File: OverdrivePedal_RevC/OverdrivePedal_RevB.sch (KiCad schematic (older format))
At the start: 25 parts, among them J1 AudioJack2-Connector, J2 Barrel_Jack, J3 Conn_01x05, J4 SW_SPST, J6 AudioJack2-Connector, U1 DG468DV_T1_E3, U2 TL071, U4 DG468DV_T1_E3, U5 STM32L011D4Px, U6 DG468DV_T1_E3

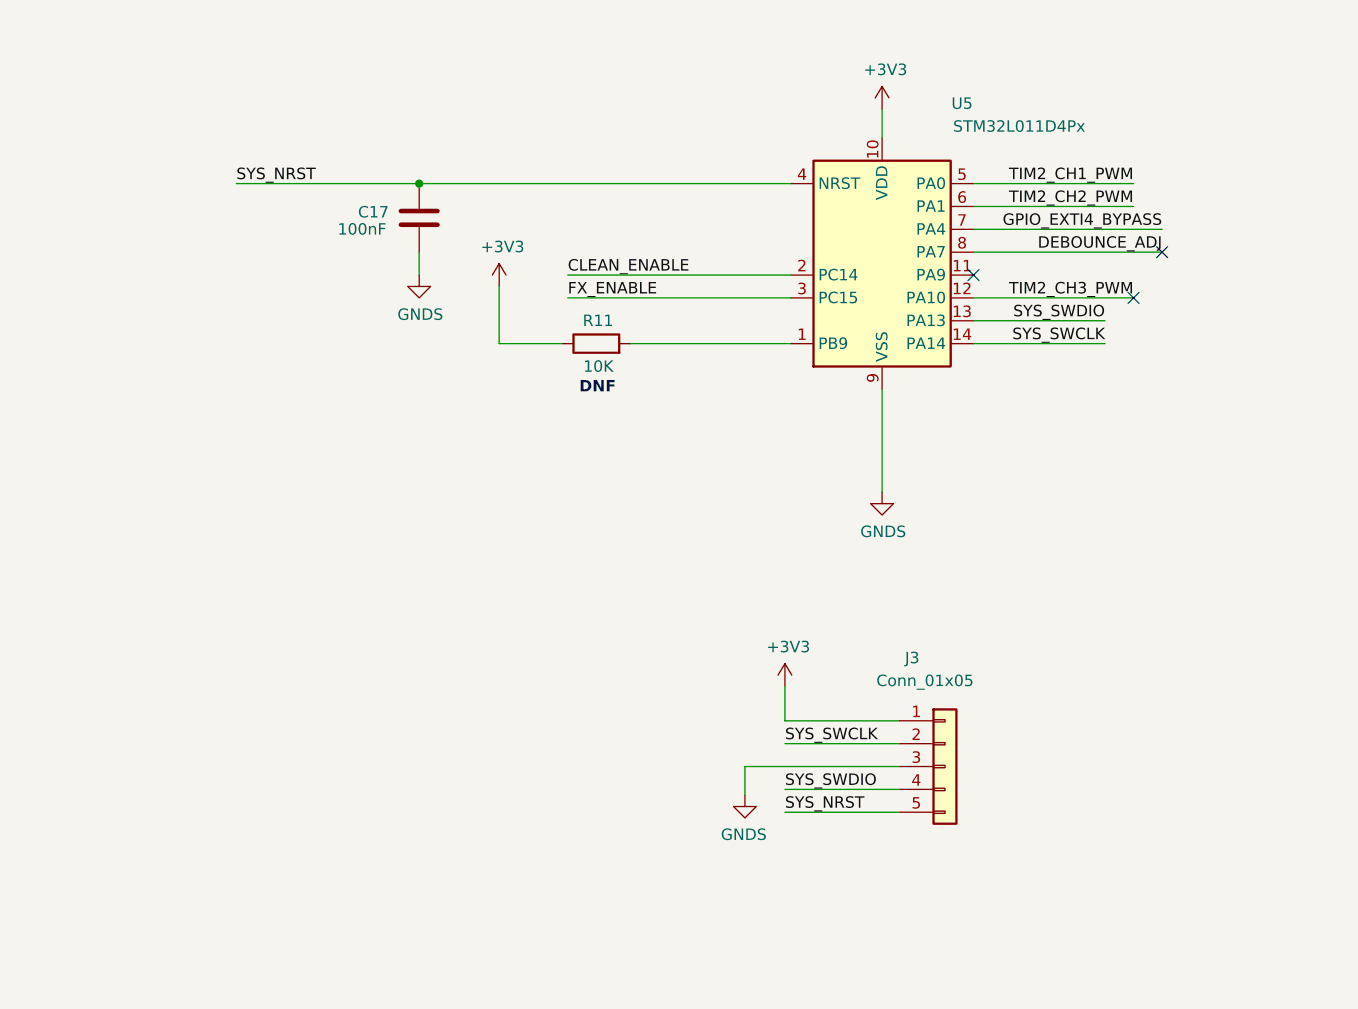
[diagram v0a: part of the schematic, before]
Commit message: updated revc
- Switch PC15 to PA9 for FX_ENABLE
- connected BOOT0 to GND
- Removed U11 charge pump (not required/causing oscillation)
- lowered U3 charge pump LP filter cuttoff to 1.6KHz
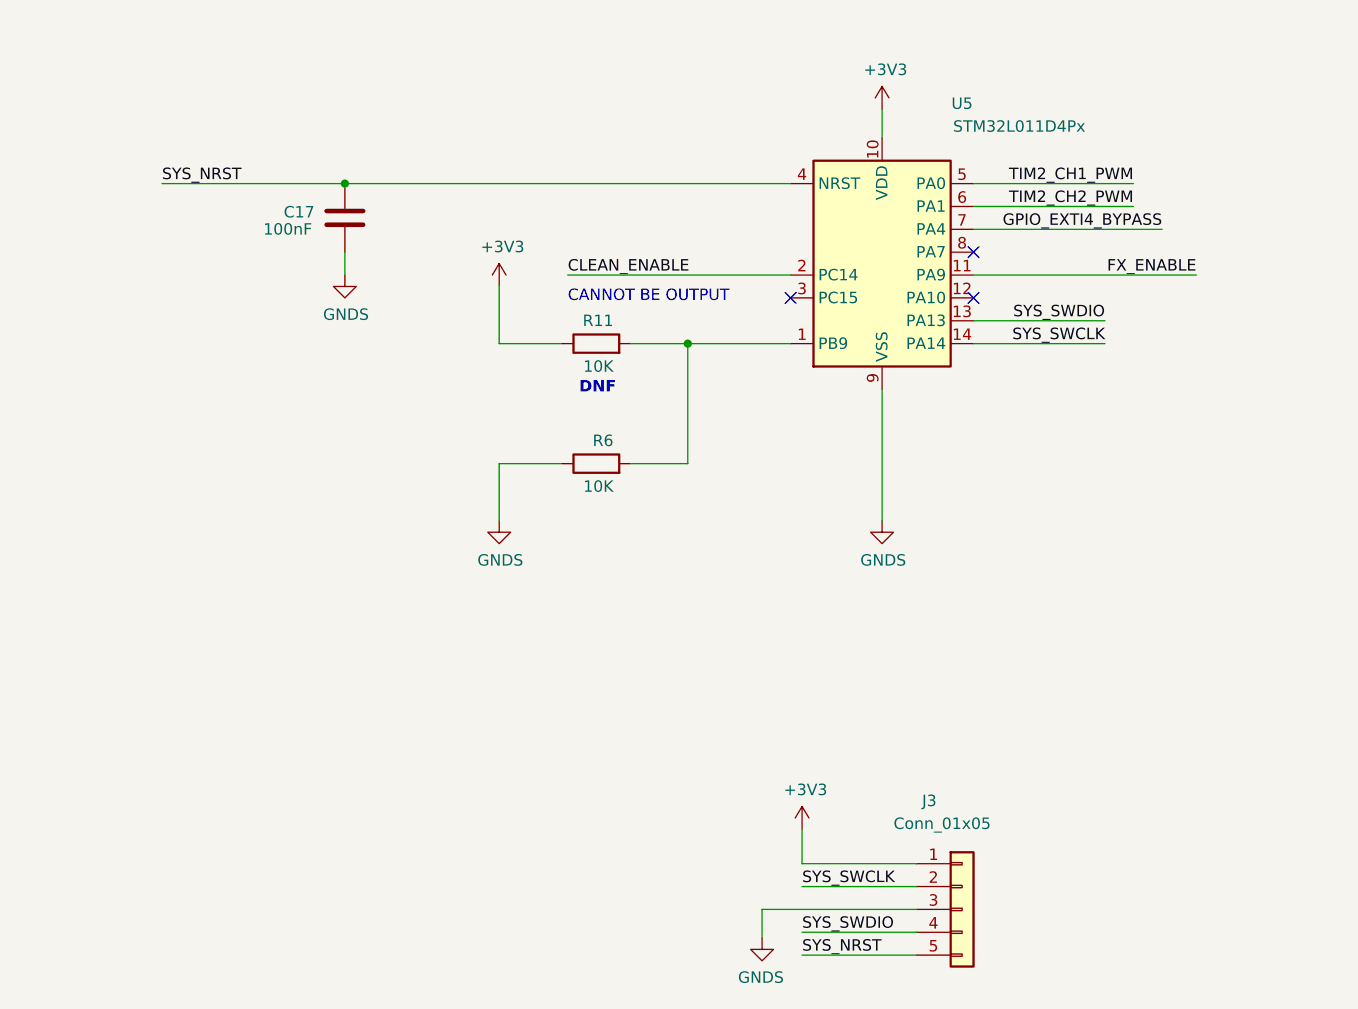
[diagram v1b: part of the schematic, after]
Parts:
- added R6: 10K, Resistor_SMD:R_0402_1005Metric, symbol Device:R
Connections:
- net FX_ENABLE: now also U5.11 (PA9); no longer U5.3 (PC15)
- net GNDS: now also R6.1
- net at R11.2, U5.1 (PB9): now also R6.2
- net DEBOUNCE_ADJ: no longer names the net of U5.8 (PA7)
- net TIM2_CH3_PWM: no longer names the net of U5.12 (PA10)
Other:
- note added: "CANNOT BE OUTPUT"
- moved on the sheet: C17, J3
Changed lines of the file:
@@
 Title "Microcontroller"
 Date "2020-04-10"
-Rev "RevB"
+Rev "RevC"
 Comp ""
-Comment1 "PC15 must be initialised HIGH to prevent debugger lockup"
+Comment1 ""
 Comment2 ""
 Comment3 ""
@@
 L power:GNDS #PWR026
 U 1 1 5F03E5C2
-P 8600 8425
-F 0 "#PWR026" H 8600 8175 50  0001 C CNN
-F 1 "GNDS" H 8605 8252 50  0000 C CNN
-F 2 "" H 8600 8425 50  0001 C CNN
-F 3 "" H 8600 8425 50  0001 C CNN
-	1    8600 8425
-	1    0    0    -1
-$EndComp
-Wire Wire Line
-	9000 7575 9700 7575
-Text Label 9700 7575 2    50   ~ 0
-TIM2_CH3_PWM
+P 8600 8550
+F 0 "#PWR026" H 8600 8300 50  0001 C CNN
+F 1 "GNDS" H 8605 8377 50  0000 C CNN
+F 2 "" H 8600 8550 50  0001 C CNN
+F 3 "" H 8600 8550 50  0001 C CNN
+	1    8600 8550
+	1    0    0    -1
+$EndComp
 Wire Wire Line
 	9000 7775 9575 7775
@@
 Text Label 9825 7275 2    50   ~ 0
 GPIO_EXTI4_BYPASS
-NoConn ~ 9000 7475
 Text Label 7225 7475 0    50   ~ 0
 CLEAN_ENABLE
-Text Label 7225 7575 0    50   ~ 0
+Text Label 9975 7475 2    50   ~ 0
 FX_ENABLE
 $Comp
@@
 L Connector_Generic:Conn_01x05 J3
 U 1 1 5F17BC8C
-P 8875 9625
-F 0 "J3" H 8700 10100 50  0000 L CNN
-F 1 "Conn_01x05" H 8575 10000 50  0000 L CNN
-F 2 "Connector_PinSocket_2.54mm:PinSocket_1x05_P2.54mm_Vertical" H 8875 9625 50  0001 C CNN
-F 3 "~" H 8875 9625 50  0001 C CNN
-	1    8875 9625
-	1    0    0    -1
-$EndComp
-Wire Wire Line
-	8675 9425 8175 9425
-Wire Wire Line
-	8675 9525 8175 9525
-Wire Wire Line
-	8675 9625 8000 9625
-Wire Wire Line
-	8675 9725 8175 9725
-Wire Wire Line
-	8675 9825 8175 9825
-Wire Wire Line
-	8175 9275 8175 9425
+P 8950 10250
+F 0 "J3" H 8775 10725 50  0000 L CNN
+F 1 "Conn_01x05" H 8650 10625 50  0000 L CNN
+F 2 "Connector_PinSocket_2.54mm:PinSocket_1x05_P2.54mm_Vertical" H 8950 10250 50  0001 C CNN
+F 3 "~" H 8950 10250 50  0001 C CNN
+	1    8950 10250
+	1    0    0    -1
+$EndComp
+Wire Wire Line
+	8750 10050 8250 10050
+Wire Wire Line
+	8750 10150 8250 10150
+Wire Wire Line
+	8750 10250 8075 10250
+Wire Wire Line
+	8750 10350 8250 10350
+Wire Wire Line
+	8750 10450 8250 10450
+Wire Wire Line
+	8250 9900 8250 10050
 $Comp
 L power:+3V3 #PWR034
 U 1 1 5F18C62E
-P 8175 9275
-F 0 "#PWR034" H 8175 9125 50  0001 C CNN
-F 1 "+3V3" H 8190 9448 50  0000 C CNN
-F 2 "" H 8175 9275 50  0001 C CNN
-F 3 "" H 8175 9275 50  0001 C CNN
-	1    8175 9275
-	1    0    0    -1
-$EndComp
-Wire Wire Line
-	8000 9625 8000 9750
+P 8250 9900
+F 0 "#PWR034" H 8250 9750 50  0001 C CNN
+F 1 "+3V3" H 8265 10073 50  0000 C CNN
+F 2 "" H 8250 9900 50  0001 C CNN
+F 3 "" H 8250 9900 50  0001 C CNN
+	1    8250 9900
+	1    0    0    -1
+$EndComp
+Wire Wire Line
+	8075 10250 8075 10375
 $Comp
 L power:GNDS #PWR?
 U 1 1 5F18FF3A
-P 8000 9750
+P 8075 10375
 AR Path="/5E6165F4/5F18FF3A" Ref="#PWR?"  Part="1"
 AR Path="/5F18FF3A" Ref="#PWR033"  Part="1"
-F 0 "#PWR033" H 8000 9500 50  0001 C CNN
-F 1 "GNDS" H 8005 9577 50  0000 C CNN
-F 2 "" H 8000 9750 50  0001 C CNN
-F 3 "" H 8000 9750 50  0001 C CNN
-	1    8000 9750
+F 0 "#PWR033" H 8075 10125 50  0001 C CNN
+F 1 "GNDS" H 8080 10202 50  0000 C CNN
+F 2 "" H 8075 10375 50  0001 C CNN
+F 3 "" H 8075 10375 50  0001 C CNN
+	1    8075 10375
 	-1   0    0    -1
 $EndComp
-Text Label 8175 9525 0    50   ~ 0
+Text Label 8250 10150 0    50   ~ 0
 SYS_SWCLK
-Text Label 8175 9725 0    50   ~ 0
+Text Label 8250 10350 0    50   ~ 0
 SYS_SWDIO
-Text Label 8175 9825 0    50   ~ 0
+Text Label 8250 10450 0    50   ~ 0
 SYS_NRST
 Wire Wire Line
@@
 	3475 3500 3000 3500
 Wire Wire Line
-	9000 7375 9825 7375
-Text Label 9825 7375 2    50   ~ 0
-DEBOUNCE_ADJ
-Wire Wire Line
 	4600 3250 5625 3250
 $Sheet
@@
 	1    0    0    -1
 $EndComp
-NoConn ~ 9700 7575
 Wire Wire Line
 	8425 2900 8425 3050
@@
 Text Notes 3250 3925 0    50   ~ 10
 DNF
-NoConn ~ 9825 7375
-Wire Wire Line
-	8600 7975 8600 8425
+Wire Wire Line
+	8600 7975 8600 8550
 Text Label 9700 7075 2    50   ~ 0
 TIM2_CH1_PWM
@@
 	8200 7475 7225 7475
 Wire Wire Line
-	8200 7575 7225 7575
+	9000 7475 9975 7475
 $Comp
 L Connector:TestPoint TP?
@@
 	11950 3425 11425 3425
 Wire Wire Line
-	6575 7075 8200 7075
-Connection ~ 6575 7075
-Wire Wire Line
-	6575 7475 6575 7375
+	6250 7075 8200 7075
+Connection ~ 6250 7075
+Wire Wire Line
+	6250 7475 6250 7375
 $Comp
 L power:GNDS #PWR0102
 U 1 1 5EBF5962
-P 6575 7475
-F 0 "#PWR0102" H 6575 7225 50  0001 C CNN
-F 1 "GNDS" H 6580 7302 50  0000 C CNN
-F 2 "" H 6575 7475 50  0001 C CNN
-F 3 "" H 6575 7475 50  0001 C CNN
-	1    6575 7475
-	1    0    0    -1
-$EndComp
-Wire Wire Line
-	5775 7075 6575 7075
+P 6250 7475
+F 0 "#PWR0102" H 6250 7225 50  0001 C CNN
+F 1 "GNDS" H 6255 7302 50  0000 C CNN
+F 2 "" H 6250 7475 50  0001 C CNN
+F 3 "" H 6250 7475 50  0001 C CNN
+	1    6250 7475
+	1    0    0    -1
+$EndComp
+Wire Wire Line
+	5450 7075 6250 7075
 $Comp
 L Device:C C17
 U 1 1 5EBE9AF3
-P 6575 7225
-F 0 "C17" H 6775 7200 50  0000 C CNN
-F 1 "100nF" H 6825 7275 50  0000 C CNN
-F 2 "Capacitor_SMD:C_0402_1005Metric" H 6613 7075 50  0001 C CNN
-F 3 "~" H 6575 7225 50  0001 C CNN
-	1    6575 7225
+P 6250 7225
+F 0 "C17" H 6450 7200 50  0000 C CNN
+F 1 "100nF" H 6500 7275 50  0000 C CNN
+F 2 "Capacitor_SMD:C_0402_1005Metric" H 6288 7075 50  0001 C CNN
+F 3 "~" H 6250 7225 50  0001 C CNN
+	1    6250 7225
 	-1   0    0    1
 $EndComp
-Text Label 5775 7075 0    50   ~ 0
+Text Label 5450 7075 0    50   ~ 0
 SYS_NRST
 $Comp
@@
 $EndComp
 Wire Wire Line
-	7500 7775 8200 7775
+	7500 7775 7750 7775
 Wire Wire Line
 	6925 7775 7200 7775
@@
 Text Notes 7275 8000 0    50   ~ 10
 DNF
+NoConn ~ 8200 7575
+NoConn ~ 9000 7375
+NoConn ~ 9000 7575
+Text Notes 7225 7600 0    50   ~ 0
+CANNOT BE OUTPUT
+$Comp
+L Device:R R6
+U 1 1 5E92EBB9
+P 7350 8300
+F 0 "R6" V 7450 8225 50  0000 L CNN
+F 1 "10K" V 7250 8225 50  0000 L CNN
+F 2 "Resistor_SMD:R_0402_1005Metric" V 7280 8300 50  0001 C CNN
+F 3 "~" H 7350 8300 50  0001 C CNN
+	1    7350 8300
+	0    -1   -1   0
+$EndComp
+Wire Wire Line
+	7500 8300 7750 8300
+Wire Wire Line
+	7750 8300 7750 7775
+Connection ~ 7750 7775
+Wire Wire Line
+	7750 7775 8200 7775
+Wire Wire Line
+	7200 8300 6925 8300
+Wire Wire Line
+	6925 8300 6925 8550
+$Comp
+L power:GNDS #PWR0101
+U 1 1 5E93579A
+P 6925 8550
+F 0 "#PWR0101" H 6925 8300 50  0001 C CNN
+F 1 "GNDS" H 6930 8377 50  0000 C CNN
+F 2 "" H 6925 8550 50  0001 C CNN
+F 3 "" H 6925 8550 50  0001 C CNN
+	1    6925 8550
+	1    0    0    -1
+$EndComp
 $EndSCHEMATC
